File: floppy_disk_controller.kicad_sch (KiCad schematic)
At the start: 64 parts, among them J1 Conn_02x18_Odd_Even, U15 L78L05_TO92

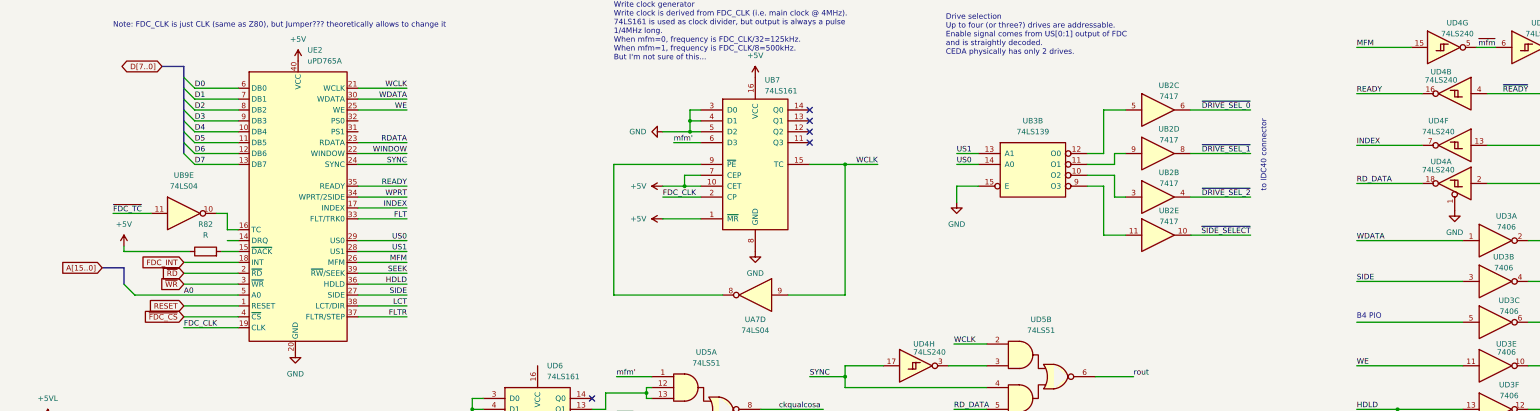
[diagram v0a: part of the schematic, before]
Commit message: pcb and sch: finished routing and fixing connections
There are still some minor inconsistencies (/WR, /RD, one PRINTER
signal), some passives missing (decoupling caps, power stage), but the
schematic and the pcb should be more or less complete.
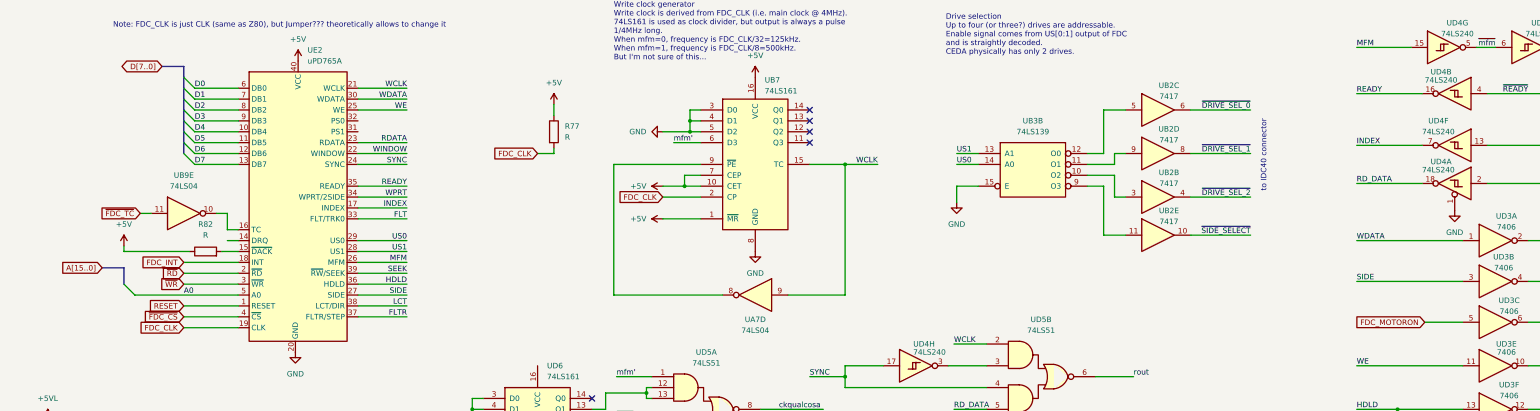
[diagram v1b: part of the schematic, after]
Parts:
- added R77: R, Resistor_THT:R_Axial_DIN0309_L9.0mm_D3.2mm_P12.70mm_Horizontal, symbol Device:R
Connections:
- net +5V: now also R77.1
- net FDC_CLK: now also R77.2
- net FDC_MOTORON: now reaches UD3.5
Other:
- note removed: "B4 PIO"

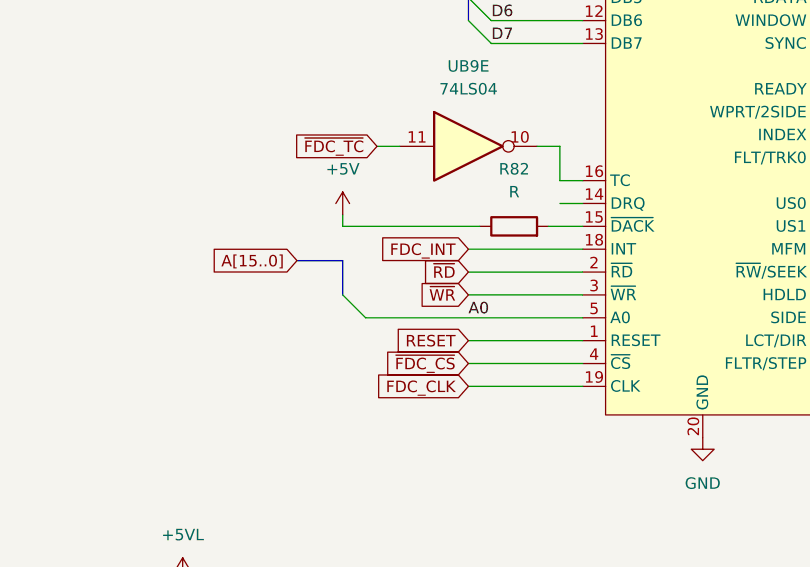
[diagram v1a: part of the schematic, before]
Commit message: sch: fixed fdc rd/wr signals, ported in pcb too
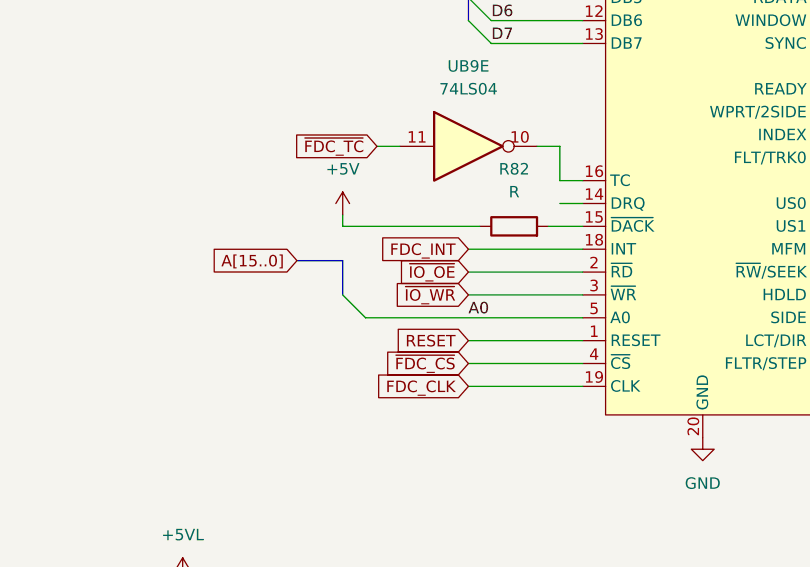
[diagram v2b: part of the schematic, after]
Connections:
- net ~{RD} renamed ~{IO_OE}
- net ~{WR} renamed ~{IO_WR}
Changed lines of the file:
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@@
 		)
 	)
-	(global_label "~{RD}"
+	(global_label "~{IO_OE}"
 		(shape input)
 		(at 31.75 77.47 180)
@@
 		)
 		(property "Intersheetrefs" "${INTERSHEET_REFS}"
-			(at 26.2248 77.47 0)
+			(at 23.3824 77.47 0)
 			(effects
 				(font
@@
 		)
 	)
-	(global_label "~{WR}"
+	(global_label "~{IO_WR}"
 		(shape input)
 		(at 31.75 80.01 180)
@@
 		)
 		(property "Intersheetrefs" "${INTERSHEET_REFS}"
-			(at 26.0434 80.01 0)
+			(at 23.1405 80.01 0)
 			(effects
 				(font

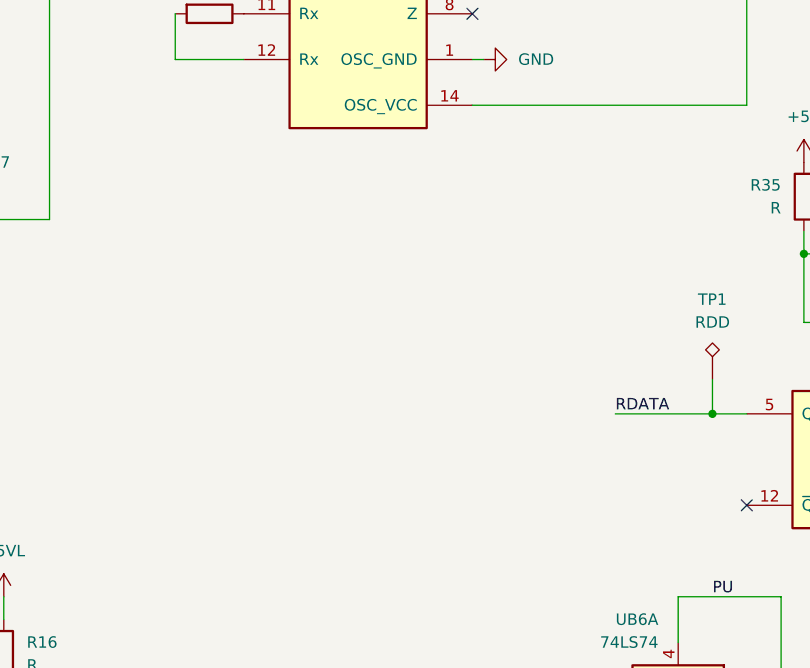
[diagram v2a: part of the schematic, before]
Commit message: pcb: fixed traces
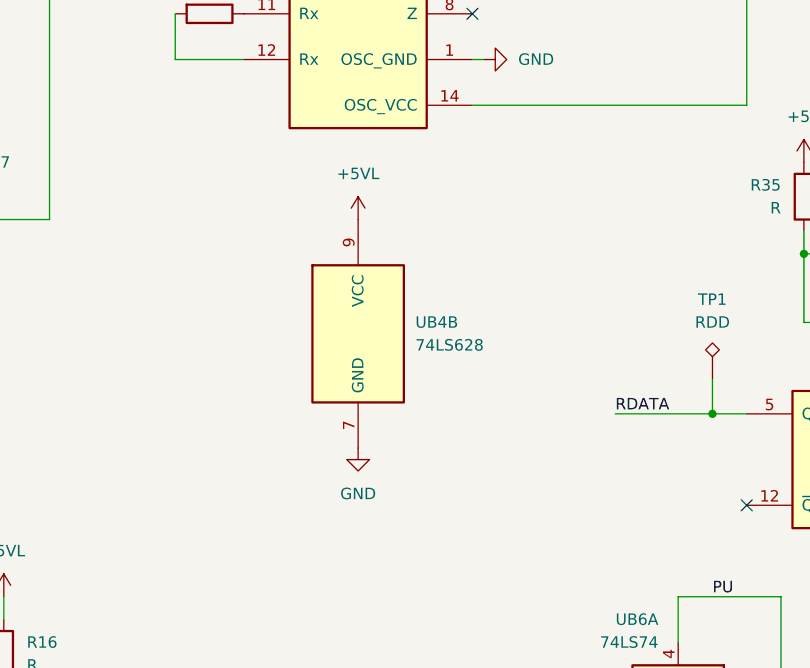
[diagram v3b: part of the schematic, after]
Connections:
- net +5VL: now also UB4.9 (VCC)
- net GND: now also UB4.7 (GND)
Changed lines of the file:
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@@
 	(symbol
 		(lib_id "ceda:74LS628")
+		(at 40.64 180.34 0)
+		(unit 2)
+		(exclude_from_sim no)
+		(in_bom yes)
+		(on_board yes)
+		(dnp no)
+		(fields_autoplaced yes)
+		(property "Reference" "UB4"
+			(at 46.99 179.0699 0)
+			(effects
+				(font
+					(size 1.27 1.27)
+				)
+				(justify left)
+			)
+		)
+		(property "Value" "74LS628"
+			(at 46.99 181.6099 0)
+			(effects
+				(font
+					(size 1.27 1.27)
+				)
+				(justify left)
+			)
+		)
+		(property "Footprint" "Package_DIP:DIP-14_W7.62mm"
+			(at 40.64 175.26 0)
+			(effects
+				(font
+					(size 1.27 1.27)
+				)
+				(hide yes)
+			)
+		)
+		(property "Datasheet" "http://www.ti.com/lit/gpn/sn74LS629"
+			(at 40.64 175.26 0)
+			(effects
+				(font
+					(size 1.27 1.27)
+				)
+				(hide yes)
+			)
+		)
+		(property "Description" ""
+			(at 40.64 180.34 0)
+			(effects
+				(font
+					(size 1.27 1.27)
+				)
+			)
+		)
+		(pin "1"
+		)
+		(pin "11"
+		)
+		(pin "12"
+		)
+		(pin "13"
+		)
+		(pin "14"
+		)
+		(pin "2"
+		)
+		(pin "3"
+		)
+		(pin "4"
+		)
+		(pin "5"
+		)
+		(pin "6"
+		)
+		(pin "8"
+		)
+		(pin "7"
+		)
+		(pin "9"
+		)
+		(instances
+			(project "ceda"
+				(path "/12a6dbe3-008d-4c5b-88f6-9f1c816060be/30cc577a-62cc-4eb0-beb7-81a864bc3256"
+					(reference "UB4")
+					(unit 2)
+				)
+			)
+		)
+	)
+	(symbol
+		(lib_id "ceda:74LS628")
 		(at 40.64 139.7 0)
 		(unit 1)
@@
 	(symbol
 		(lib_id "power:GND")
+		(at 40.64 193.04 0)
+		(unit 1)
+		(exclude_from_sim no)
+		(in_bom yes)
+		(on_board yes)
+		(dnp no)
+		(fields_autoplaced yes)
+		(property "Reference" "#PWR0276"
+			(at 40.64 199.39 0)
+			(effects
+				(font
+					(size 1.27 1.27)
+				)
+				(hide yes)
+			)
+		)
+		(property "Value" "GND"
+			(at 40.64 198.12 0)
+			(effects
+				(font
+					(size 1.27 1.27)
+				)
+			)
+		)
+		(property "Footprint" ""
+			(at 40.64 193.04 0)
+			(effects
+				(font
+					(size 1.27 1.27)
+				)
+				(hide yes)
+			)
+		)
+		(property "Datasheet" ""
+			(at 40.64 193.04 0)
+			(effects
+				(font
+					(size 1.27 1.27)
+				)
+				(hide yes)
+			)
+		)
+		(property "Description" ""
+			(at 40.64 193.04 0)
+			(effects
+				(font
+					(size 1.27 1.27)
+				)
+			)
+		)
+		(pin "1"
+		)
+		(instances
+			(project "ceda"
+				(path "/12a6dbe3-008d-4c5b-88f6-9f1c816060be/30cc577a-62cc-4eb0-beb7-81a864bc3256"
+					(reference "#PWR0276")
+					(unit 1)
+				)
+			)
+		)
+	)
+	(symbol
+		(lib_id "power:GND")
 		(at 327.025 144.78 0)
 		(unit 1)
@@
 					(unit 1)
 				)
+			)
+		)
+	)
+	(symbol
+		(lib_id "power:+5VL")
+		(at 40.64 167.64 0)
+		(unit 1)
+		(exclude_from_sim no)
+		(in_bom yes)
+		(on_board yes)
+		(dnp no)
+		(fields_autoplaced yes)
+		(property "Reference" "#PWR0275"
+			(at 40.64 171.45 0)
+			(effects
+				(font
+					(size 1.27 1.27)
+				)
+				(hide yes)
+			)
+		)
+		(property "Value" "+5VL"
+			(at 40.64 162.56 0)
+			(effects
+				(font
+					(size 1.27 1.27)
+				)
+			)
+		)
+		(property "Footprint" ""
+			(at 40.64 167.64 0)
+			(effects
+				(font
+					(size 1.27 1.27)
+				)
+				(hide yes)
+			)
+		)
+		(property "Datasheet" ""
+			(at 40.64 167.64 0)
+			(effects
+				(font
+					(size 1.27 1.27)
+				)
+				(hide yes)
+			)
+		)
+		(property "Description" ""
+			(at 40.64 167.64 0)
+			(effects
+				(font
+					(size 1.27 1.27)
+				)
+			)
+		)
+		(pin "1"
+		)
+		(instances
+			(project "ceda"
+				(path "/12a6dbe3-008d-4c5b-88f6-9f1c816060be/30cc577a-62cc-4eb0-beb7-81a864bc3256"
+					(reference "#PWR0275")
+					(unit 1)
+				)

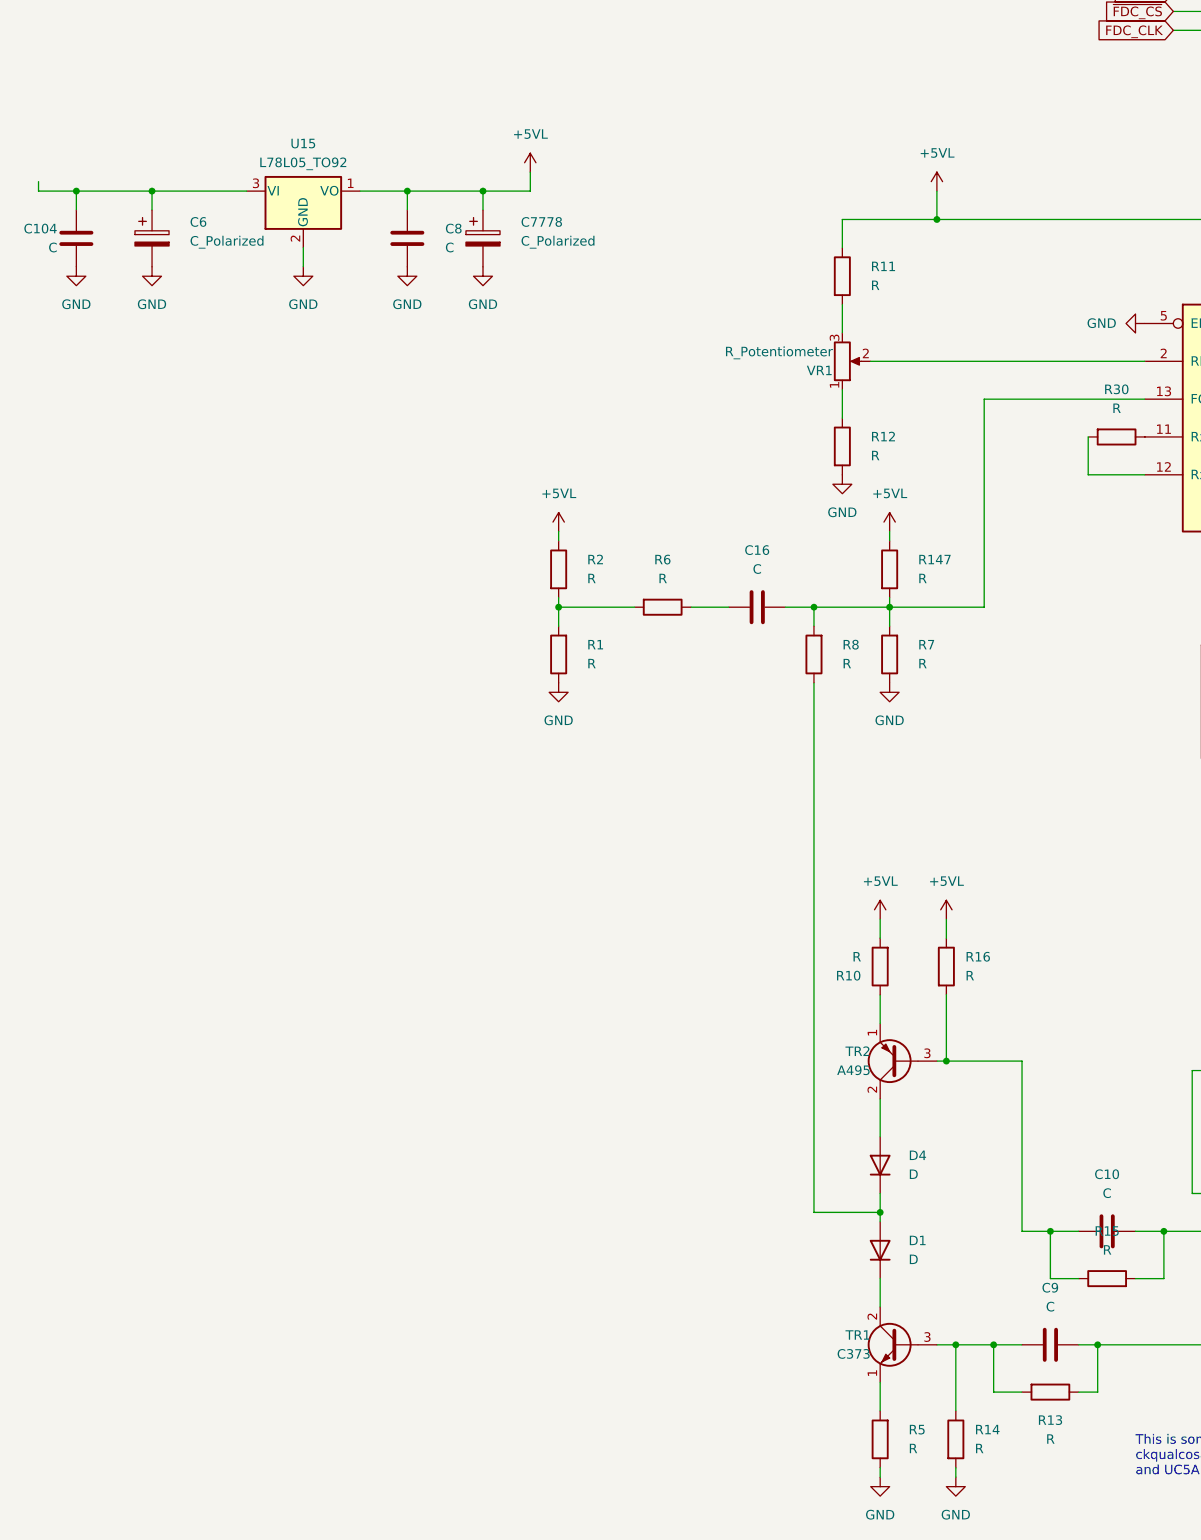
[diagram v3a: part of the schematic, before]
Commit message: pcb: added power in caps, reordered ref no, fixed power traces
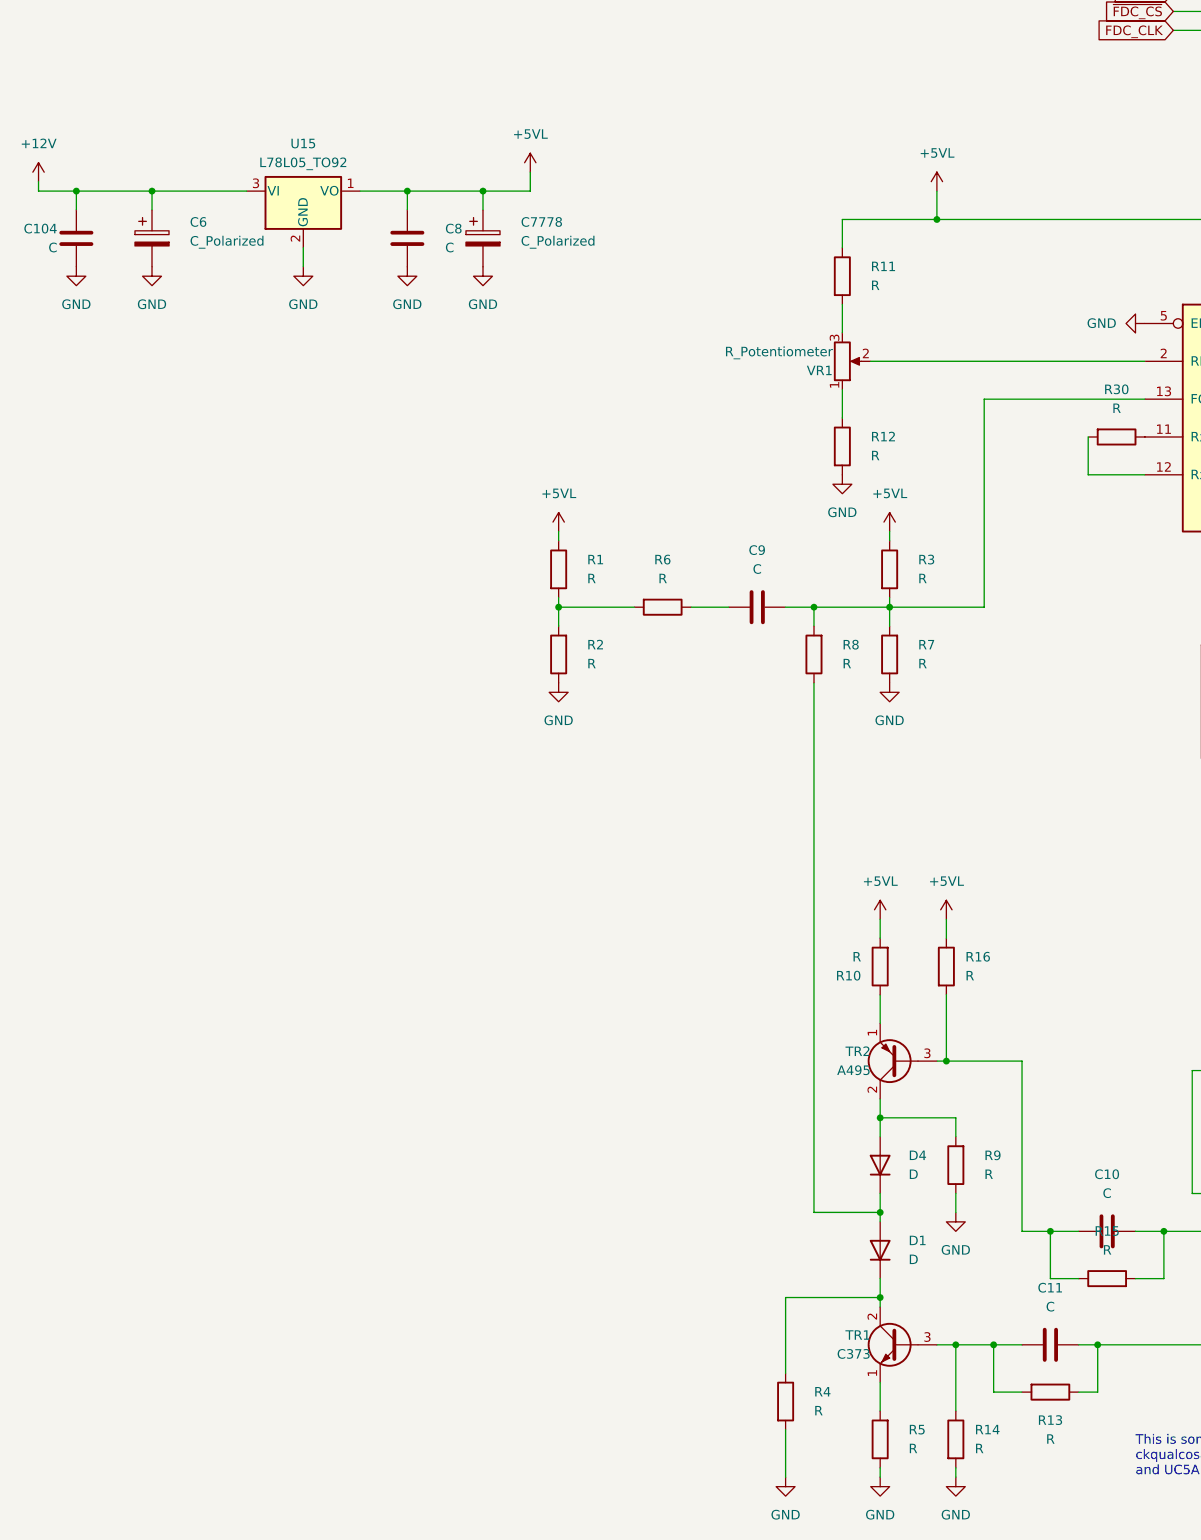
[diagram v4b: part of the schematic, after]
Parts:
- added R4, R9: R, Resistor_THT:R_Axial_DIN0204_L3.6mm_D1.6mm_P5.08mm_Vertical, symbol Device:R
- added unit 1 of UB4
- renumbered C9 to C11, C16 to C9, R2 to R1, R1 to R2, R147 to R3
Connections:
- net +5VL: now also UB4.14 (OSC_VCC); no longer UB4.14 (OSC_VCC)
- net GND: now also R4.2, R9.1, UB4.1 (OSC_GND), UB4.5 (EN); no longer UB4.1 (OSC_GND), UB4.5 (EN)
- net PLL_CLK: now also UB4.6 (Y); no longer UB4.6 (Y)
- net at D1.1 (K), TR1.2 (C): now also R4.1
- net +12V: now reaches C104.1, C6.1, U15.3 (VI)
- net at D4.2 (A), TR2.2 (C): now also R9.2
- net at R30.1: now also UB4.11 (Rx); no longer UB4.11 (Rx)
- net at R30.2: now also UB4.12 (Rx); no longer UB4.12 (Rx)
- net at C9.2, R3.2, R7.2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: now also UB4.13 (FC); no longer UB4.13 (FC)
- net at VR1.2: now also UB4.2 (RNG); no longer UB4.2 (RNG)
- net at C20.2: now also UB4.3 (CX1); no longer UB4.3 (CX1)
- net at C20.1: now also UB4.4 (CX2); no longer UB4.4 (CX2)
